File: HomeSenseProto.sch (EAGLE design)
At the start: 24 parts, among them IC1 ESP12SMT

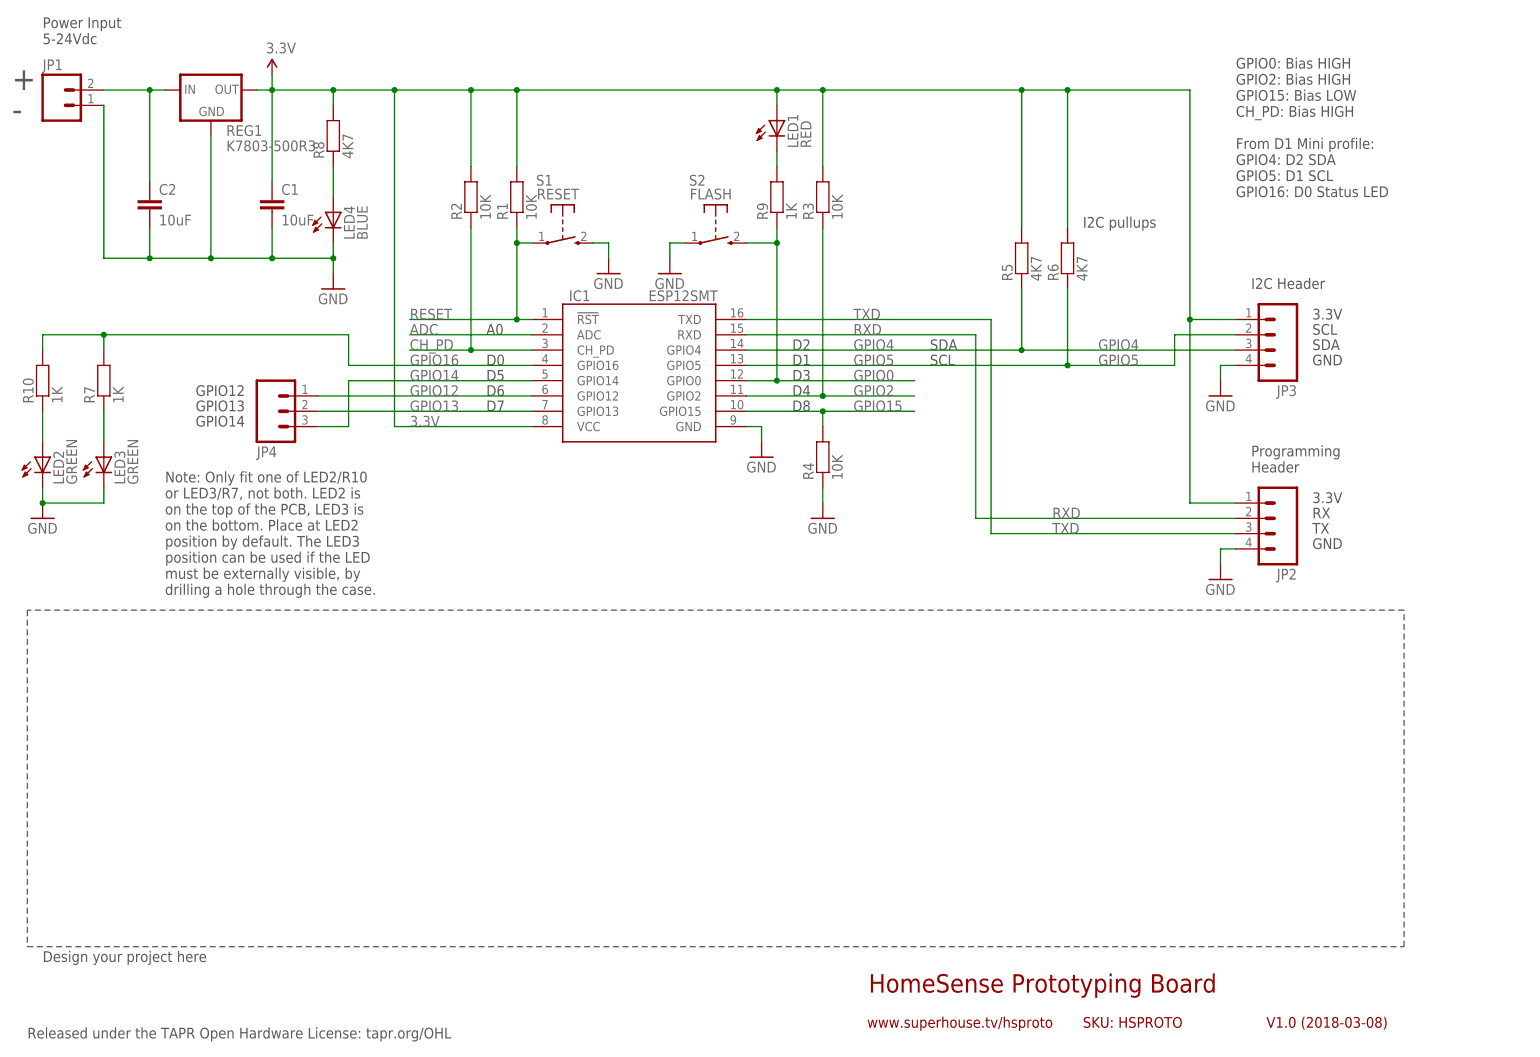
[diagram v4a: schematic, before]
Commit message: Fixed footprint for ESP12 with correct GPIO4/5
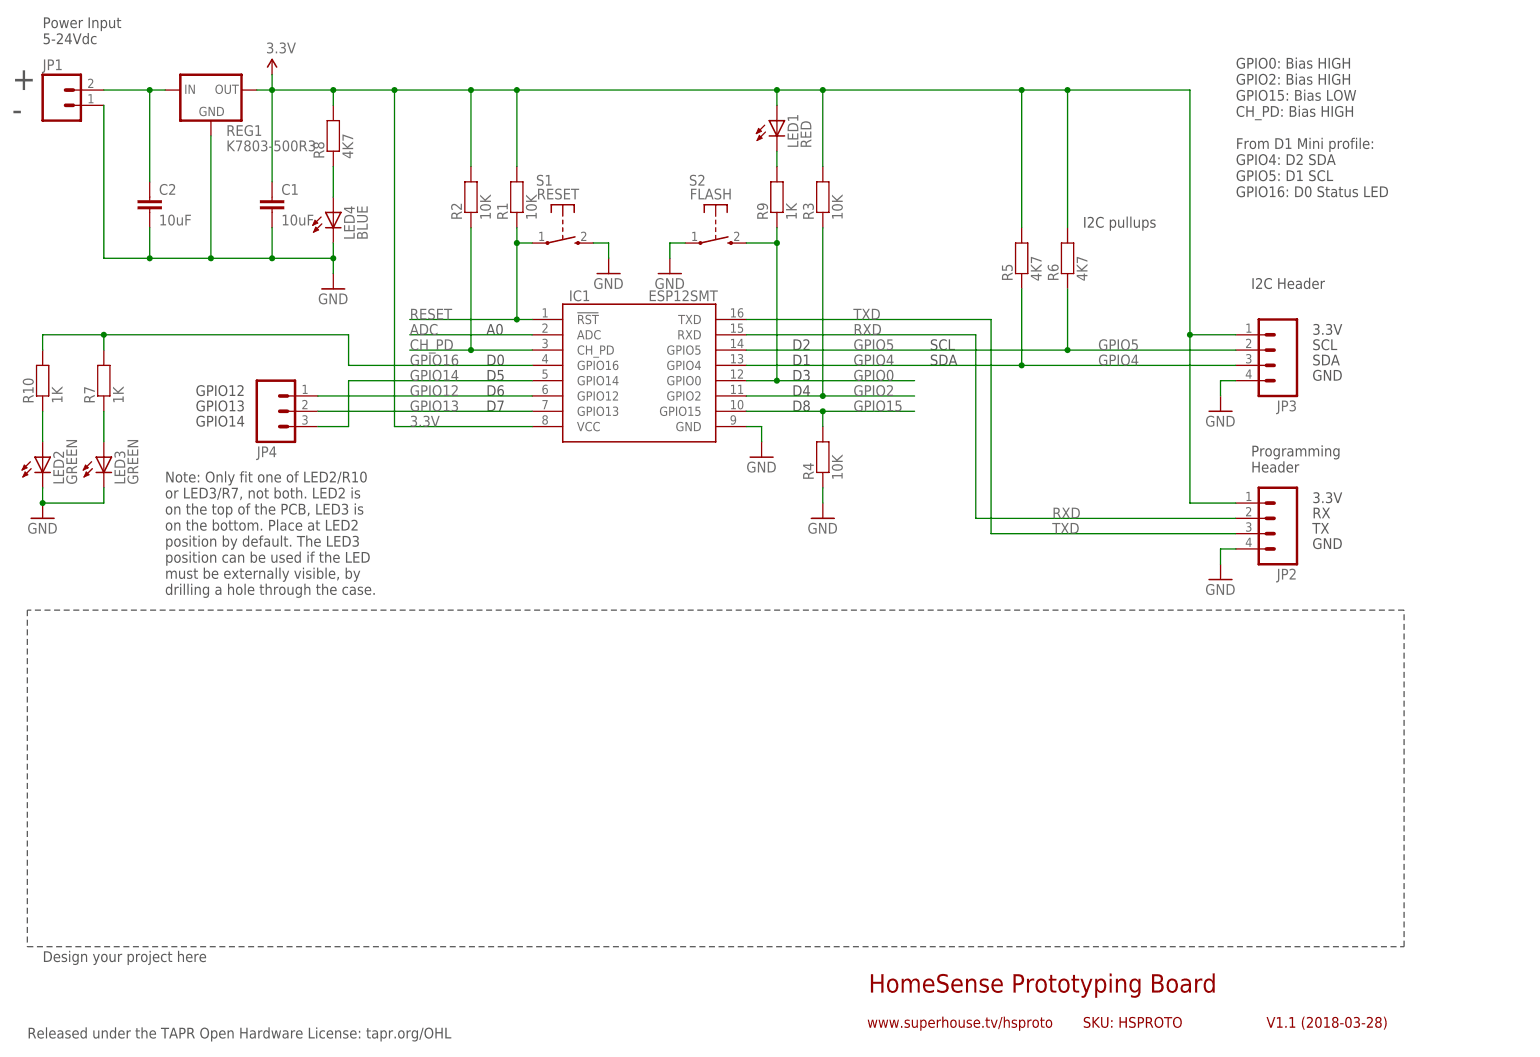
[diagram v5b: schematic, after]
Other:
- note added: "V1.1 (2018-03-28)"
- note removed: "V1.0 (2018-03-08)"
- moved on the sheet: JP3
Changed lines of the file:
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@@
 <?xml version="1.0" encoding="utf-8"?>
 <!DOCTYPE eagle SYSTEM "eagle.dtd">
-<eagle version="8.6.0">
+<eagle version="8.7.0">
 <drawing>
 <settings>
@@
 <plain>
 <text x="149.86" y="12.7" size="3.048" layer="94">HomeSense Prototyping Board</text>
-<text x="215.9" y="6.858" size="1.778" layer="94">V1.0 (2018-03-08)</text>
+<text x="215.9" y="6.858" size="1.778" layer="94">V1.1 (2018-03-28)</text>
 <text x="149.606" y="6.858" size="1.778" layer="94">www.superhouse.tv/hsproto</text>
 <frame x1="0" y1="0" x2="248.92" y2="185.42" columns="8" rows="5" layer="94"/>
@@
 <text x="7.62" y="162.56" size="3.81" layer="97">+</text>
 <text x="7.62" y="157.48" size="3.81" layer="97">-</text>
-<text x="223.52" y="124.46" size="1.778" layer="97">3.3V</text>
-<text x="223.52" y="119.38" size="1.778" layer="97">SDA</text>
-<text x="223.52" y="121.92" size="1.778" layer="97">SCL</text>
-<text x="223.52" y="116.84" size="1.778" layer="97">GND</text>
+<text x="223.52" y="121.92" size="1.778" layer="97">3.3V</text>
+<text x="223.52" y="116.84" size="1.778" layer="97">SDA</text>
+<text x="223.52" y="119.38" size="1.778" layer="97">SCL</text>
+<text x="223.52" y="114.3" size="1.778" layer="97">GND</text>
 <text x="213.36" y="99.06" size="1.778" layer="97">Programming
 Header</text>
@@
 <text x="38.1" y="111.76" size="1.778" layer="97">GPIO12</text>
 <text x="38.1" y="109.22" size="1.778" layer="97">GPIO13</text>
-<text x="160.02" y="116.84" size="1.778" layer="97">SCL</text>
-<text x="160.02" y="119.38" size="1.778" layer="97">SDA</text>
+<text x="160.02" y="119.38" size="1.778" layer="97">SCL</text>
+<text x="160.02" y="116.84" size="1.778" layer="97">SDA</text>
 </plain>
 <instances>
@@
 <instance part="GND5" gate="1" x="142.24" y="91.44"/>
 <instance part="C1" gate="G$1" x="50.8" y="142.24"/>
-<instance part="GND7" gate="1" x="208.28" y="111.76"/>
+<instance part="GND7" gate="1" x="208.28" y="109.22"/>
 <instance part="R5" gate="G$1" x="175.26" y="134.62" rot="R90"/>
 <instance part="R6" gate="G$1" x="182.88" y="134.62" rot="R90"/>
@@
 <instance part="REG1" gate="G$1" x="40.64" y="162.56"/>
 <instance part="GND2" gate="1" x="116.84" y="132.08"/>
-<instance part="JP3" gate="G$1" x="215.9" y="121.92" rot="R180"/>
+<instance part="JP3" gate="G$1" x="215.9" y="119.38" rot="R180"/>
 <instance part="LED3" gate="G$1" x="22.86" y="101.6"/>
 <instance part="R7" gate="G$1" x="22.86" y="114.3" rot="R90"/>
@@
 <segment>
 <pinref part="JP3" gate="G$1" pin="4"/>
-<wire x1="210.82" y1="116.84" x2="208.28" y2="116.84" width="0.1524" layer="91"/>
+<wire x1="210.82" y1="114.3" x2="208.28" y2="114.3" width="0.1524" layer="91"/>
 <pinref part="GND7" gate="1" pin="GND"/>
-<wire x1="208.28" y1="116.84" x2="208.28" y2="114.3" width="0.1524" layer="91"/>
+<wire x1="208.28" y1="114.3" x2="208.28" y2="111.76" width="0.1524" layer="91"/>
 </segment>
 </net>
@@
 <segment>
 <pinref part="IC1" gate="G$1" pin="GPIO4"/>
+<label x="147.32" y="116.84" size="1.778" layer="95"/>
+<wire x1="129.54" y1="116.84" x2="175.26" y2="116.84" width="0.1524" layer="91"/>
+<pinref part="R5" gate="G$1" pin="1"/>
+<wire x1="175.26" y1="116.84" x2="210.82" y2="116.84" width="0.1524" layer="91"/>
+<wire x1="175.26" y1="129.54" x2="175.26" y2="116.84" width="0.1524" layer="91"/>
+<junction x="175.26" y="116.84"/>
+<label x="187.96" y="116.84" size="1.778" layer="95"/>
+<pinref part="JP3" gate="G$1" pin="3"/>
+</segment>
+</net>
+<net name="GPIO5" class="0">
+<segment>
+<pinref part="IC1" gate="G$1" pin="GPIO5"/>
 <label x="147.32" y="119.38" size="1.778" layer="95"/>
-<wire x1="129.54" y1="119.38" x2="175.26" y2="119.38" width="0.1524" layer="91"/>
-<pinref part="R5" gate="G$1" pin="1"/>
-<wire x1="175.26" y1="119.38" x2="210.82" y2="119.38" width="0.1524" layer="91"/>
-<wire x1="175.26" y1="129.54" x2="175.26" y2="119.38" width="0.1524" layer="91"/>
-<junction x="175.26" y="119.38"/>
+<wire x1="129.54" y1="119.38" x2="182.88" y2="119.38" width="0.1524" layer="91"/>
+<pinref part="R6" gate="G$1" pin="1"/>
+<wire x1="182.88" y1="129.54" x2="182.88" y2="119.38" width="0.1524" layer="91"/>
+<junction x="182.88" y="119.38"/>
+<wire x1="210.82" y1="119.38" x2="182.88" y2="119.38" width="0.1524" layer="91"/>
 <label x="187.96" y="119.38" size="1.778" layer="95"/>
-<pinref part="JP3" gate="G$1" pin="3"/>
-</segment>
-</net>
-<net name="GPIO5" class="0">
-<segment>
-<pinref part="IC1" gate="G$1" pin="GPIO5"/>
-<label x="147.32" y="116.84" size="1.778" layer="95"/>
-<wire x1="129.54" y1="116.84" x2="182.88" y2="116.84" width="0.1524" layer="91"/>
-<pinref part="R6" gate="G$1" pin="1"/>
-<wire x1="182.88" y1="129.54" x2="182.88" y2="116.84" width="0.1524" layer="91"/>
-<junction x="182.88" y="116.84"/>
-<wire x1="200.66" y1="116.84" x2="182.88" y2="116.84" width="0.1524" layer="91"/>
-<label x="187.96" y="116.84" size="1.778" layer="95"/>
-<wire x1="200.66" y1="116.84" x2="200.66" y2="121.92" width="0.1524" layer="91"/>
 <pinref part="JP3" gate="G$1" pin="2"/>
-<wire x1="200.66" y1="121.92" x2="210.82" y2="121.92" width="0.1524" layer="91"/>
 </segment>
 </net>
@@
 <label x="73.66" y="106.68" size="1.778" layer="95"/>
 <pinref part="JP3" gate="G$1" pin="1"/>
-<wire x1="203.2" y1="93.98" x2="203.2" y2="124.46" width="0.1524" layer="91"/>
-<wire x1="203.2" y1="124.46" x2="203.2" y2="162.56" width="0.1524" layer="91"/>
-<wire x1="210.82" y1="124.46" x2="203.2" y2="124.46" width="0.1524" layer="91"/>
-<junction x="203.2" y="124.46"/>
+<wire x1="203.2" y1="93.98" x2="203.2" y2="121.92" width="0.1524" layer="91"/>
+<wire x1="203.2" y1="121.92" x2="203.2" y2="162.56" width="0.1524" layer="91"/>
+<wire x1="210.82" y1="121.92" x2="203.2" y2="121.92" width="0.1524" layer="91"/>
+<junction x="203.2" y="121.92"/>
 <pinref part="R8" gate="G$1" pin="2"/>
 <wire x1="60.96" y1="160.02" x2="60.96" y2="162.56" width="0.1524" layer="91"/>
